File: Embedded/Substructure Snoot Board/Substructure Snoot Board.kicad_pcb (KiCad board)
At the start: 4 copper layers, 50 x 35 mm, 37 parts, among them J1 10171746-00021LF, J2 PWR Jumper Pins, J3 L0 JST, J4 L1 JST, J5 5Vout, J6 A JST, J7 S Pins A, J8 S Pins B, J9 GNDout, U1 D0 FFC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

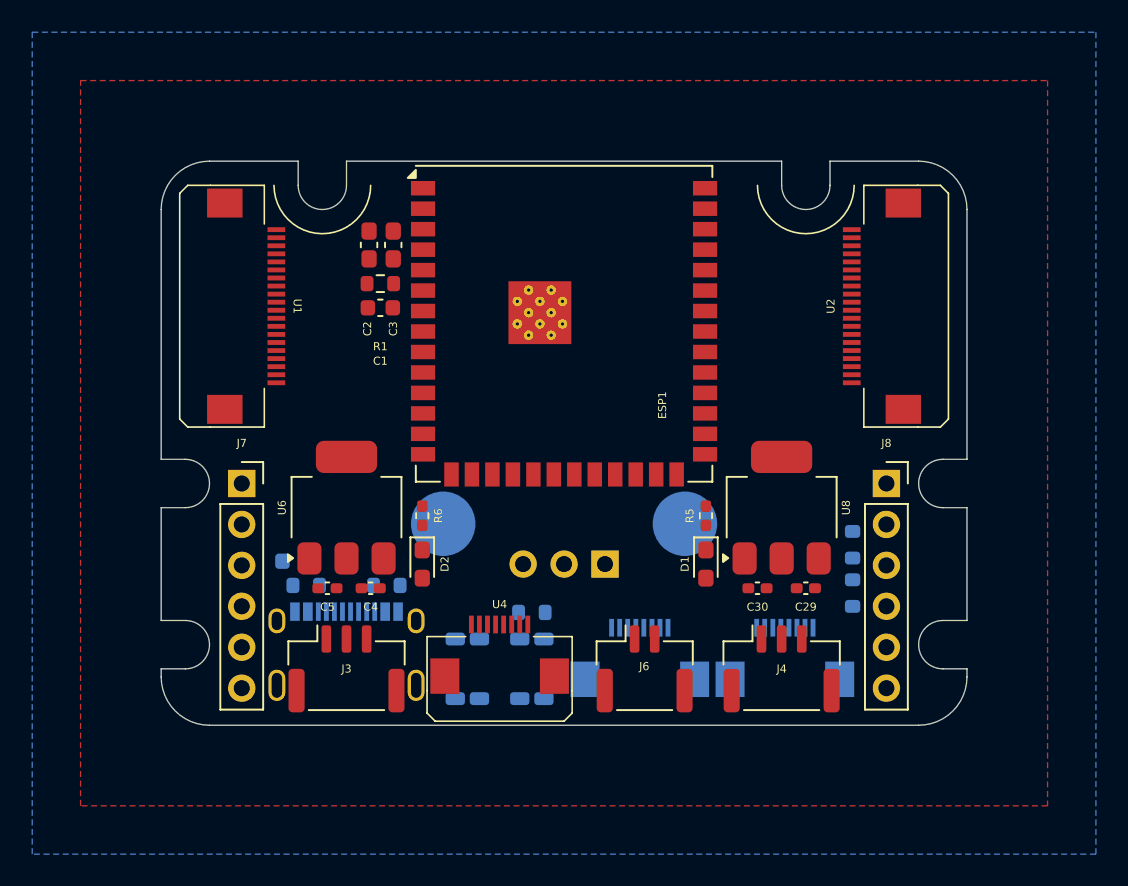
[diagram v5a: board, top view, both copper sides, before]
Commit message: Modified Component Placement to Grid
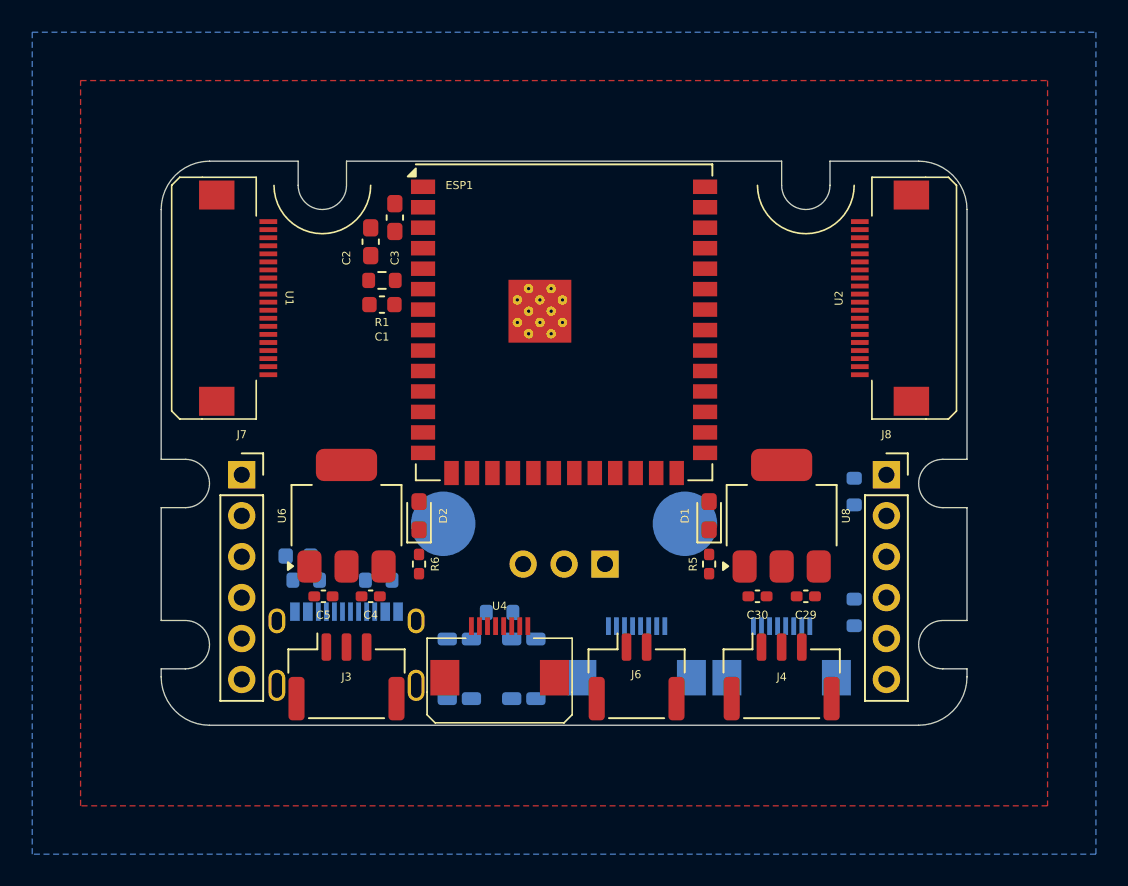
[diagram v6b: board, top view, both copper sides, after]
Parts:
- moved R8 3.30 mm to (128.0, 65.5), turned to 90 degrees
- moved D1 3.01 mm to (119.0, 67.0), turned to 90 degrees
- moved D2 3.01 mm to (101.0, 67.0), turned to 90 degrees
- moved R5 3.01 mm to (119.0, 70.0), turned to -90 degrees
- moved R6 3.01 mm to (101.0, 70.0), turned to -90 degrees
- moved R2 2.00 mm to (106.0, 73.0)
- moved C3 1.70 mm to (99.5, 48.5)
- moved R7 1.20 mm to (128.0, 73.0), turned to -90 degrees
- moved J6 0.71 mm to (114.5, 77.0)
- moved U1 0.71 mm to (91.0, 53.5)
- moved U2 0.71 mm to (129.0, 53.5)
- moved R4 0.60 mm to (98.5, 71.0)
- moved C5 0.56 mm to (95.1, 72.0)
- moved J7 0.54 mm to (90.0, 64.5)
- moved J8 0.54 mm to (130.0, 64.5)
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
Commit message: Added Routing (Simple Connections & Display Pins Start)
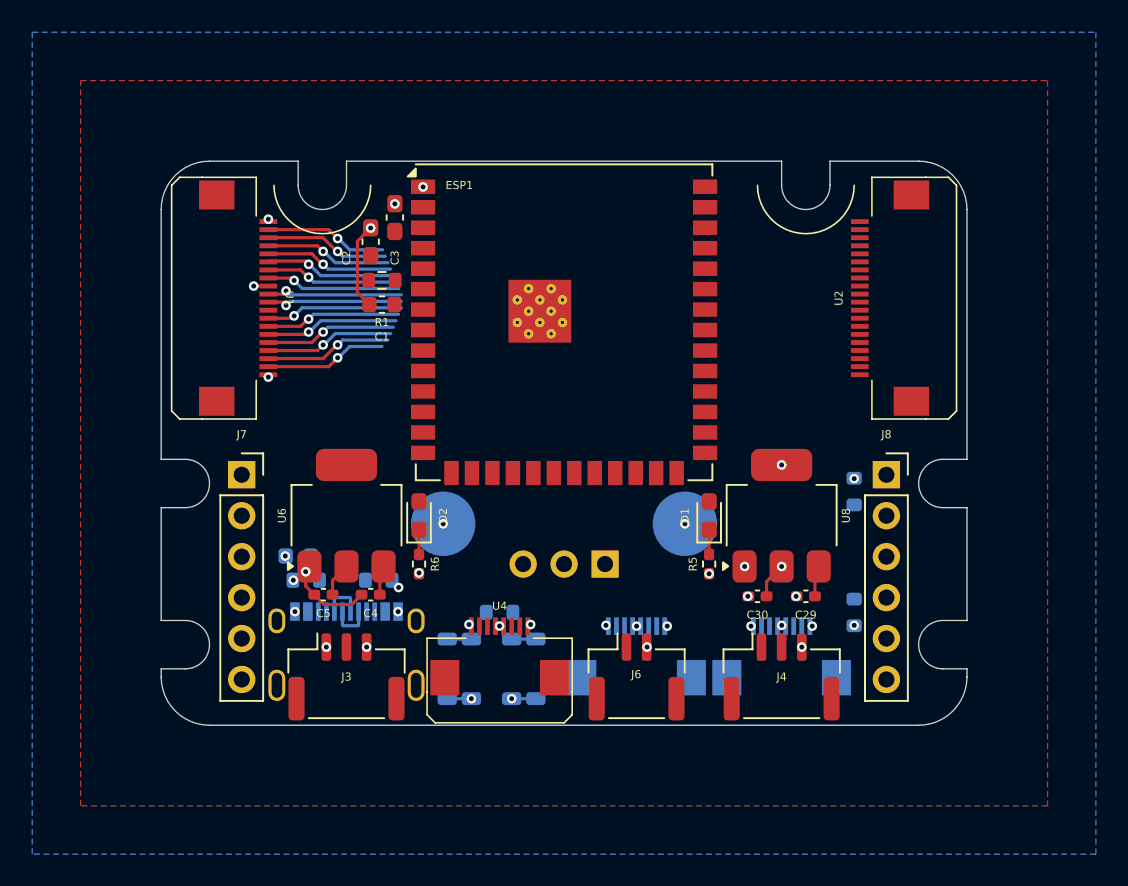
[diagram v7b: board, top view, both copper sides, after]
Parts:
- BootSW1: value SW_Push -> Boot
- RstSW1: value SW_Push -> Reset
- moved C4 0.10 mm to (98.0, 71.9)
- moved C5 0.10 mm to (95.1, 71.9)
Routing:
- net GND: track 0.00 -> 16.1 mm, vias 0 -> 30
- net Disp GPIO 9: track 0.00 -> 8.52 mm, vias 0 -> 1
- net Disp GPIO 7: track 0.00 -> 8.44 mm, vias 0 -> 1
- net Disp GPIO 8: track 0.00 -> 8.44 mm, vias 0 -> 1
- net Disp GPIO 6: track 0.00 -> 8.42 mm, vias 0 -> 1
- net Disp GPIO 10: track 0.00 -> 8.39 mm, vias 0 -> 1
- net Disp GPIO 5: track 0.00 -> 8.30 mm, vias 0 -> 1
- net Disp GPIO 11: track 0.00 -> 8.27 mm, vias 0 -> 1
- net Disp GPIO 12: track 0.00 -> 8.15 mm, vias 0 -> 1
- net Disp GPIO 4: track 0.00 -> 8.15 mm, vias 0 -> 1
- net Disp GPIO 13: track 0.00 -> 8.02 mm, vias 0 -> 1
- net Disp GPIO 3: track 0.00 -> 7.98 mm, vias 0 -> 1
- net Disp GPIO 14: track 0.00 -> 7.90 mm, vias 0 -> 1
- net Disp GPIO 2: track 0.00 -> 7.86 mm, vias 0 -> 1
- net Disp GPIO 1: track 0.00 -> 7.73 mm, vias 0 -> 1
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
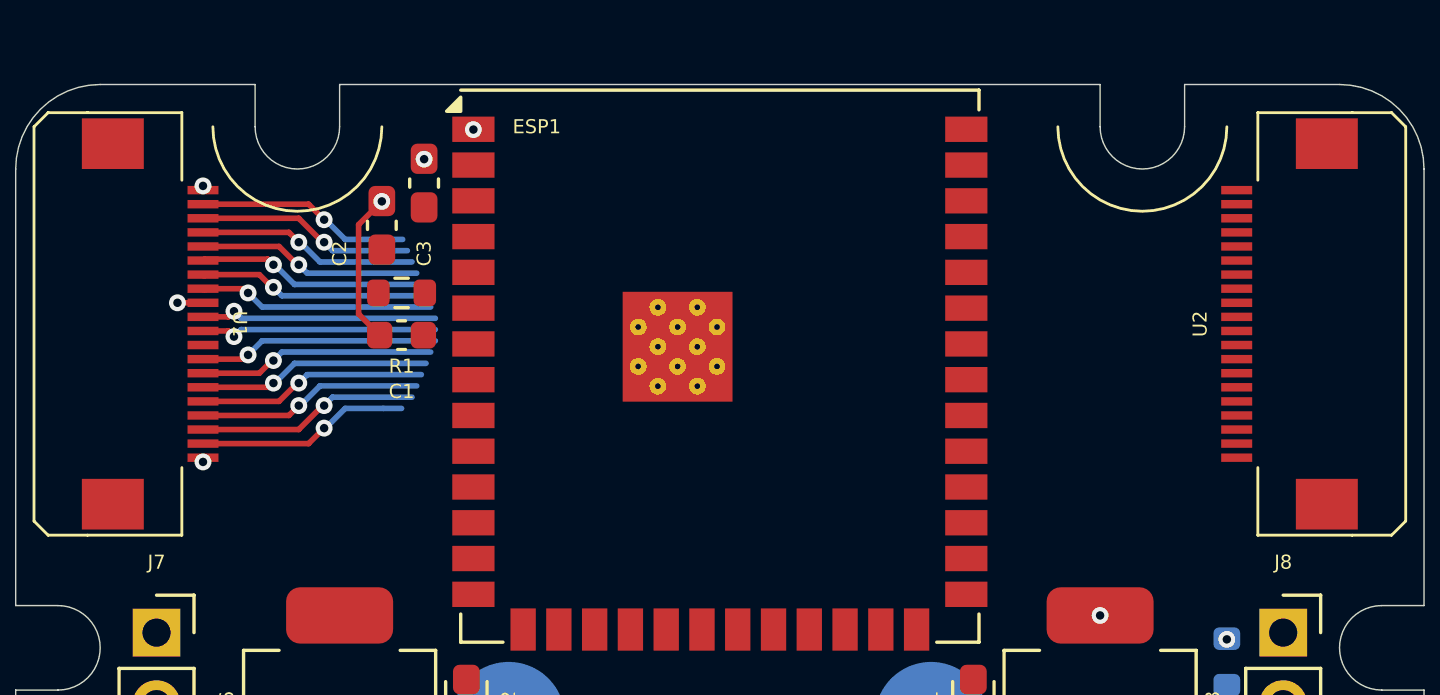
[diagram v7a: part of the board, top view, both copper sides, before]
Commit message: Added Display Signal Routing Ideation
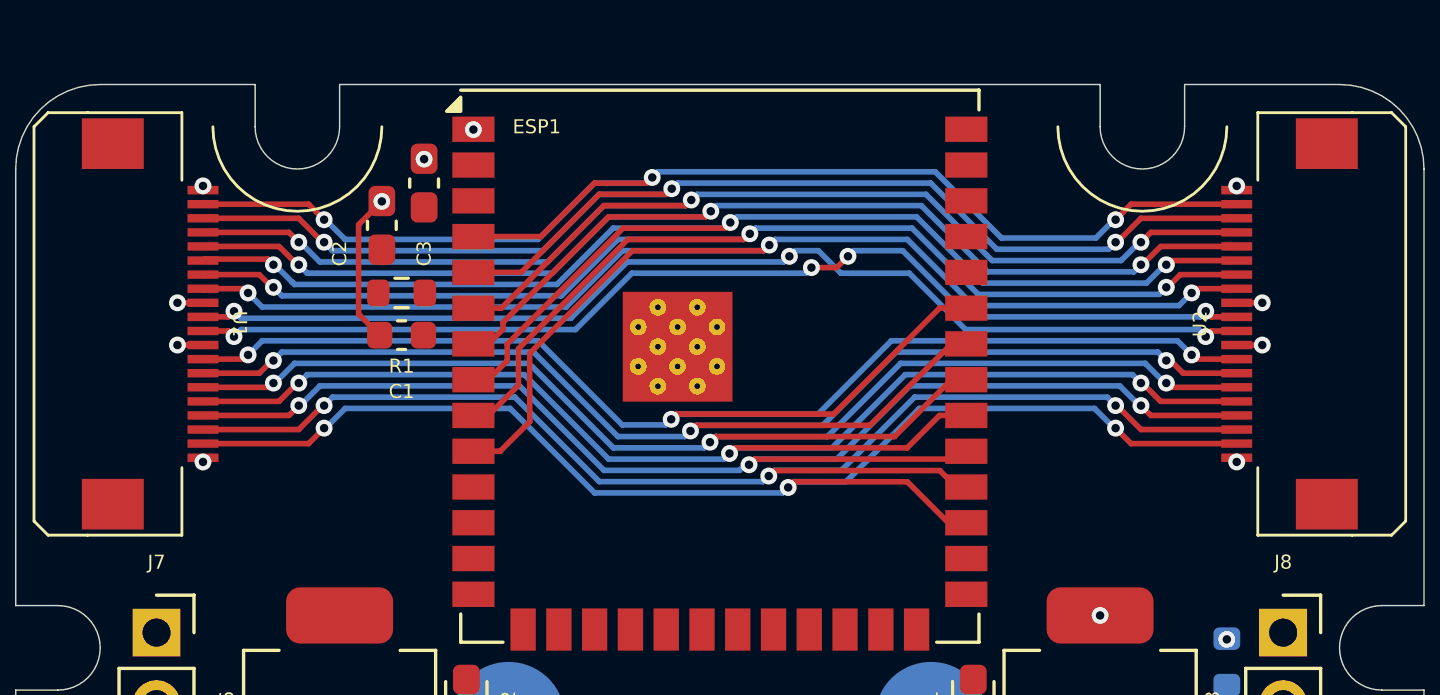
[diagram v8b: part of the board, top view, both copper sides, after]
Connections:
- ESP1 pad 10: unconnected-(ESP1-GPIO17/U1TXD/ADC2_CH6-Pad10) -> Disp GPIO 6
- ESP1 pad 29: unconnected-(ESP1-SPIIO7/GPIO36/FSPICLK/SUBSPICLK-Pad29) -> Disp GPIO 15
- ESP1 pad 30: unconnected-(ESP1-SPIDQS/GPIO37/FSPIQ/SUBSPIQ-Pad30) -> Disp GPIO 14
- ESP1 pad 31: unconnected-(ESP1-GPIO38/FSPIWP/SUBSPIWP-Pad31) -> Disp GPIO 13
- ESP1 pad 32: unconnected-(ESP1-MTCK/GPIO39/CLK_OUT3/SUBSPICS1-Pad32) -> Disp GPIO 12
- ESP1 pad 33: unconnected-(ESP1-MTDO/GPIO40/CLK_OUT2-Pad33) -> Disp GPIO 11
- ESP1 pad 34: unconnected-(ESP1-MTDI/GPIO41/CLK_OUT1-Pad34) -> Disp GPIO 10
- ESP1 pad 35: unconnected-(ESP1-MTMS/GPIO42-Pad35) -> Disp GPIO 9
- ESP1 pad 4: unconnected-(ESP1-GPIO4/TOUCH4/ADC1_CH3-Pad4) -> Disp GPIO 0
- ESP1 pad 5: unconnected-(ESP1-GPIO5/TOUCH5/ADC1_CH4-Pad5) -> Disp GPIO 1
- ESP1 pad 6: unconnected-(ESP1-GPIO6/TOUCH6/ADC1_CH5-Pad6) -> Disp GPIO 2
- ESP1 pad 7: unconnected-(ESP1-GPIO7/TOUCH7/ADC1_CH6-Pad7) -> Disp GPIO 3
- ESP1 pad 8: unconnected-(ESP1-GPIO15/U0RTS/ADC2_CH4/XTAL_32K_P-Pad8) -> Disp GPIO 4
- ESP1 pad 9: unconnected-(ESP1-GPIO16/U0CTS/ADC2_CH5/XTAL_32K_N-Pad9) -> Disp GPIO 5
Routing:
- net Disp GPIO 6: track 8.42 -> 54.2 mm, vias 1 -> 3
- net Disp GPIO 5: track 8.30 -> 52.6 mm, vias 1 -> 3
- net Disp GPIO 9: track 8.52 -> 51.8 mm, vias 1 -> 3
- net Disp GPIO 4: track 8.15 -> 51.2 mm, vias 1 -> 3
- net Disp GPIO 10: track 8.39 -> 50.9 mm, vias 1 -> 3
- net Disp GPIO 3: track 7.98 -> 50.0 mm, vias 1 -> 3
- net Disp GPIO 11: track 8.27 -> 49.9 mm, vias 1 -> 3
- net Disp GPIO 2: track 7.86 -> 48.8 mm, vias 1 -> 3
- net Disp GPIO 12: track 8.15 -> 48.9 mm, vias 1 -> 3
- net Disp GPIO 1: track 7.73 -> 47.9 mm, vias 1 -> 3
- net Disp GPIO 13: track 8.02 -> 48.0 mm, vias 1 -> 3
- net Disp GPIO 15: track 7.57 -> 47.2 mm, vias 1 -> 3
- net Disp GPIO 14: track 7.90 -> 47.5 mm, vias 1 -> 3
- net Disp GPIO 0: track 7.61 -> 46.9 mm, vias 1 -> 3
- net Disp GPIO 7: track 8.44 -> 39.2 mm, vias 1 -> 3
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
